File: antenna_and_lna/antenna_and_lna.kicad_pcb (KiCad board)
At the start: 2 copper layers, 40 x 70 mm, 17 parts, among them J1 CON-SMA-EDGE-S, J2 TSW-104-14-F-S, Q1 2SK3557

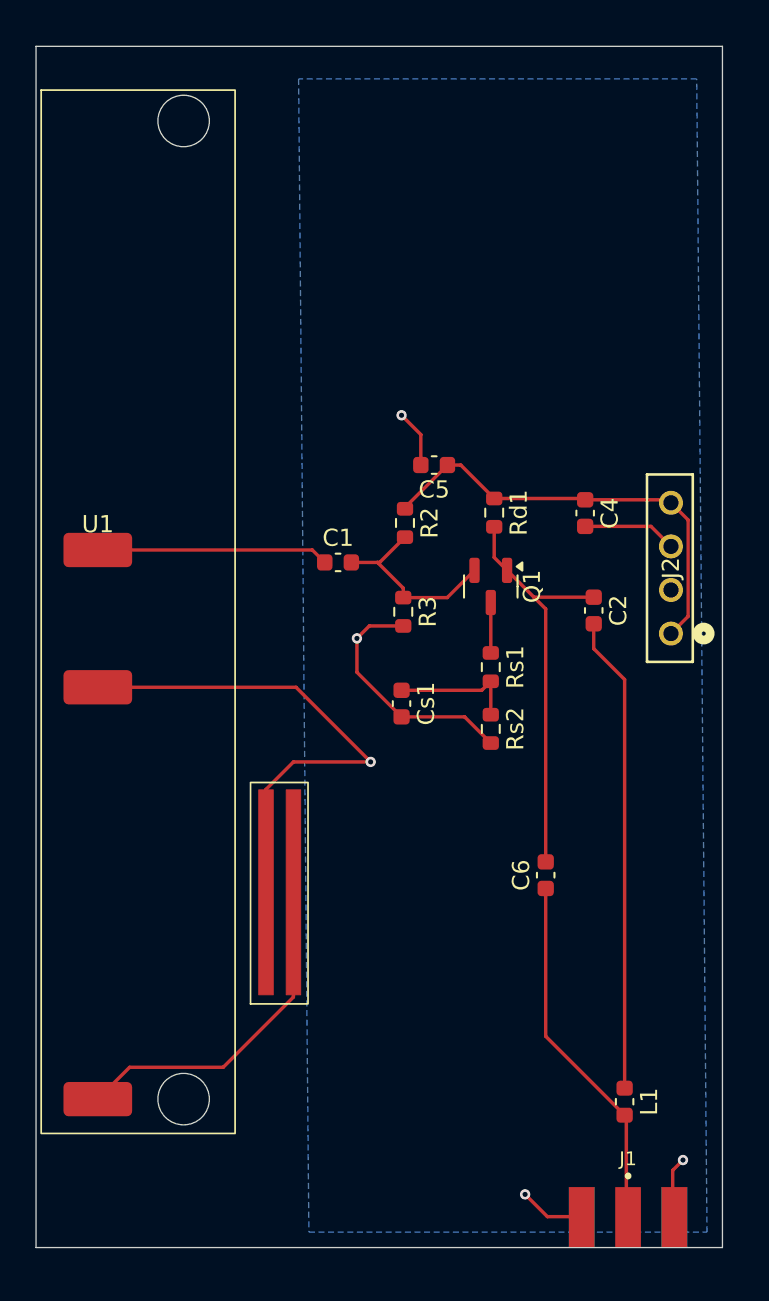
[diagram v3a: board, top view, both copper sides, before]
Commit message: Fixed edge clearance for both boards, both DRC clean
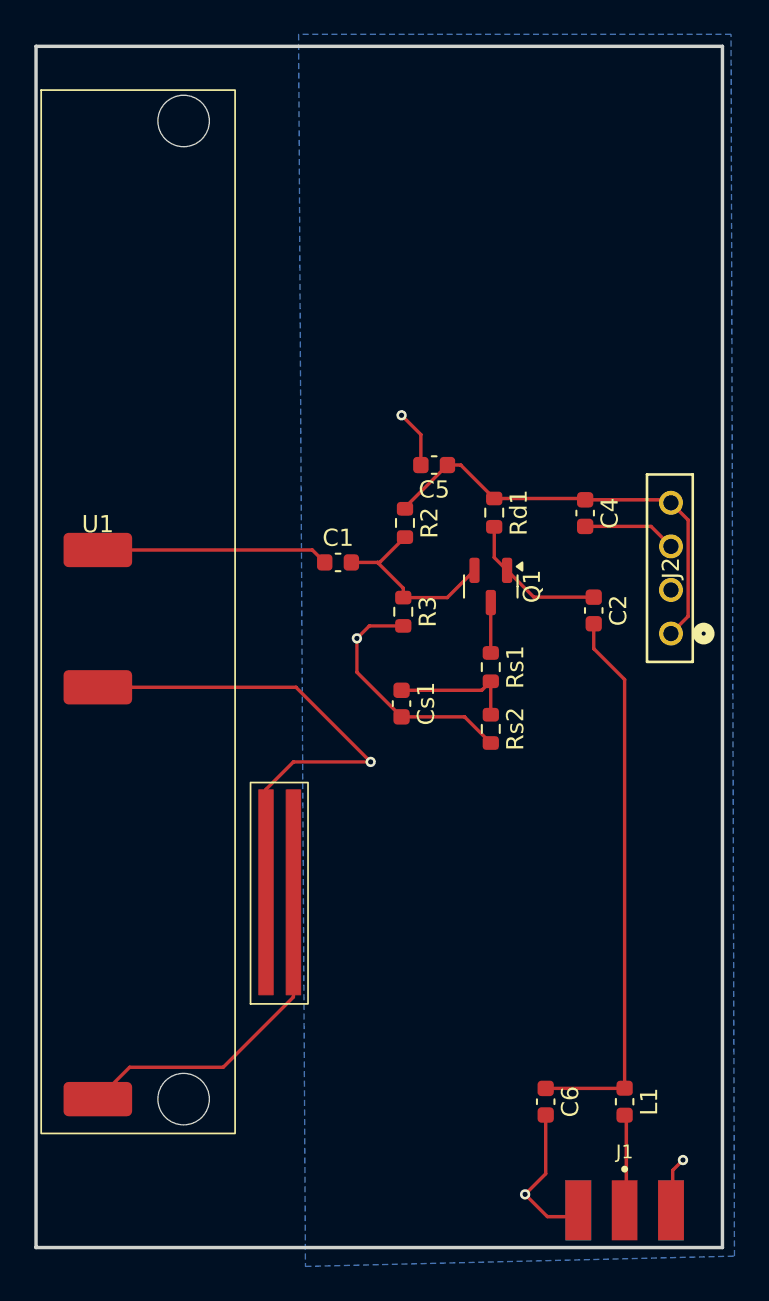
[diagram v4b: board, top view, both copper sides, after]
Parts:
- C6: value 3.3n -> 2.7 n
- L1: value 27 u -> 33 u
- moved C6 13.2 mm to (105.2, 117.6), turned to -90 degrees
- moved J1 0.45 mm to (109.8, 123.9)
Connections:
- C6 pad 1: /ant_to_main -> Net-(C2-Pad2)
- C6 pad 2: /LNA/Sigout -> GND
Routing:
- net /LNA/Sigout: track 24.3 -> 8.55 mm
- net /ant_to_main: track 20.7 -> 5.62 mm
- net GND: track 61.1 -> 66.2 mm
- net Net-(C2-Pad2): track 27.8 -> 32.4 mm
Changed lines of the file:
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@@
 	(footprint "SMA_fp:RFSOLUTIONS_CON-SMA-EDGE-S"
 		(layer "F.Cu")
-		(at 110 124.3275 90)
+		(at 109.8 123.9275 90)
 		(property "Reference" "J1"
 			(at 3.4 0 180)
@@
 			)
 		)
-		(property "Value" "27 u"
+		(property "Value" "33 u"
 			(at 0 1.43 90)
 			(layer "F.Fab")
@@
 	(footprint "Capacitor_SMD:C_0603_1608Metric"
 		(layer "F.Cu")
-		(at 105.2 104.4 90)
+		(at 105.2 117.6 -90)
 		(descr "Capacitor SMD 0603 (1608 Metric), square (rectangular) end terminal, IPC_7351 nominal, (Body size source: IPC-SM-782 page 76, https://www.pcb-3d.com/wordpress/wp-content/uploads/ipc-sm-782a_amendment_1_and_2.pdf), generated with kicad-footprint-generator")
 		(tags "capacitor")
@@
 			)
 		)
-		(property "Value" "3.3n"
+		(property "Value" "2.7 n"
 			(at 0 1.43 90)
 			(layer "F.Fab")
@@
 		)
 		(property "Datasheet" ""
-			(at 0 0 90)
+			(at 0 0 270)
 			(unlocked yes)
 			(layer "F.Fab")
@@
 		)
 		(property "Description" "Unpolarized capacitor"
-			(at 0 0 90)
+			(at 0 0 270)
 			(unlocked yes)
 			(layer "F.Fab")
@@
 		(attr smd)
 		(fp_line
-			(start -0.14058 -0.51)
-			(end 0.14058 -0.51)
+			(start -0.14058 0.51)
+			(end 0.14058 0.51)
 			(stroke
 				(width 0.12)
@@
 		)
 		(fp_line
-			(start -0.14058 0.51)
-			(end 0.14058 0.51)
+			(start -0.14058 -0.51)
+			(end 0.14058 -0.51)
 			(stroke
 				(width 0.12)
@@
 		)
 		(fp_line
-			(start 1.48 -0.73)
-			(end 1.48 0.73)
+			(start -1.48 0.73)
+			(end -1.48 -0.73)
 			(stroke
 				(width 0.05)
@@
 		)
 		(fp_line
-			(start -1.48 -0.73)
-			(end 1.48 -0.73)
+			(start 1.48 0.73)
+			(end -1.48 0.73)
 			(stroke
 				(width 0.05)
@@
 		)
 		(fp_line
-			(start 1.48 0.73)
-			(end -1.48 0.73)
+			(start -1.48 -0.73)
+			(end 1.48 -0.73)
 			(stroke
 				(width 0.05)
@@
 		)
 		(fp_line
-			(start -1.48 0.73)
-			(end -1.48 -0.73)
+			(start 1.48 -0.73)
+			(end 1.48 0.73)
 			(stroke
 				(width 0.05)
@@
 		)
 		(fp_line
-			(start 0.8 -0.4)
-			(end 0.8 0.4)
+			(start -0.8 0.4)
+			(end -0.8 -0.4)
 			(stroke
 				(width 0.1)
@@
 		)
 		(fp_line
-			(start -0.8 -0.4)
-			(end 0.8 -0.4)
+			(start 0.8 0.4)
+			(end -0.8 0.4)
 			(stroke
 				(width 0.1)
@@
 		)
 		(fp_line
-			(start 0.8 0.4)
-			(end -0.8 0.4)
+			(start -0.8 -0.4)
+			(end 0.8 -0.4)
 			(stroke
 				(width 0.1)
@@
 		)
 		(fp_line
-			(start -0.8 0.4)
-			(end -0.8 -0.4)
+			(start 0.8 -0.4)
+			(end 0.8 0.4)
 			(stroke
 				(width 0.1)
@@
 		)
 		(pad "1" smd roundrect
-			(at -0.775 0 90)
+			(at -0.775 0 270)
 			(size 0.9 0.95)
 			(layers "F.Cu" "F.Mask" "F.Paste")
 			(roundrect_rratio 0.25)
-			(net 9 "/ant_to_main")
+			(net 10 "Net-(C2-Pad2)")
 			(pintype "passive")
 		)
 		(pad "2" smd roundrect
-			(at 0.775 0 90)
+			(at 0.775 0 270)
 			(size 0.9 0.95)
 			(layers "F.Cu" "F.Mask" "F.Paste")
 			(roundrect_rratio 0.25)
-			(net 3 "/LNA/Sigout")
+			(net 6 "GND")
 			(pintype "passive")
 		)
@@
 		(end 115.5 126.1)
 		(stroke
-			(width 0.05)
+			(width 0.2)
 			(type default)
 		)
@@
 	)
 	(segment
-		(start 105.2 103.625)
-		(end 105.2 88.8875)
-		(width 0.2)
-		(layer "F.Cu")
-		(net 3)
-	)
-	(segment
 		(start 104.5125 88.2)
 		(end 108 88.2)
@@
 	)
 	(segment
-		(start 105.2 88.8875)
-		(end 104.5125 88.2)
-		(width 0.2)
-		(layer "F.Cu")
-		(net 3)
-	)
-	(segment
 		(start 102.95 86.6375)
 		(end 104.5125 88.2)
@@
 	)
 	(segment
+		(start 105.2 121.8)
+		(end 104 123)
+		(width 0.2)
+		(layer "F.Cu")
+		(net 6)
+	)
+	(segment
+		(start 105.2 118.375)
+		(end 105.2 121.8)
+		(width 0.2)
+		(layer "F.Cu")
+		(net 6)
+	)
+	(segment
 		(start 112.6 124.3)
 		(end 112.6 121.6)
@@
 	)
 	(segment
-		(start 105.2 105.175)
-		(end 105.2 113.7875)
-		(width 0.2)
+		(start 109.9 124.3)
+		(end 109.9 118.675)
+		(width 0.2032)
 		(layer "F.Cu")
 		(net 9)
 	)
 	(segment
-		(start 105.2 113.7875)
-		(end 109.8 118.3875)
+		(start 109.7875 116.825)
+		(end 109.8 116.8125)
 		(width 0.2)
 		(layer "F.Cu")
-		(net 9)
-	)
-	(segment
-		(start 109.9 124.3)
-		(end 109.9 118.675)
-		(width 0.2032)
-		(layer "F.Cu")
-		(net 9)
+		(net 10)
 	)
 	(segment
@@
 		(net 10)
 	)
+	(segment
+		(start 105.2 116.825)
+		(end 109.7875 116.825)
+		(width 0.2)
+		(layer "F.Cu")
+		(net 10)
+	)
 	(zone
 		(net 6)
@@
 		(polygon
 			(pts
-				(xy 90.8 58) (xy 91.4 125.2) (xy 114.6 125.2) (xy 114 58)
+				(xy 90.8 55.4) (xy 91.2 127.2) (xy 116.2 126.6) (xy 116 55.4)
 			)
 		)
